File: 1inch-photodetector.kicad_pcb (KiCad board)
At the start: 4 copper layers, 25 x 25 mm, 21 parts, among them J1 Conn_01x03, J2 Conn_Coaxial, U1 ADA4898-2, U2 LT3032-12

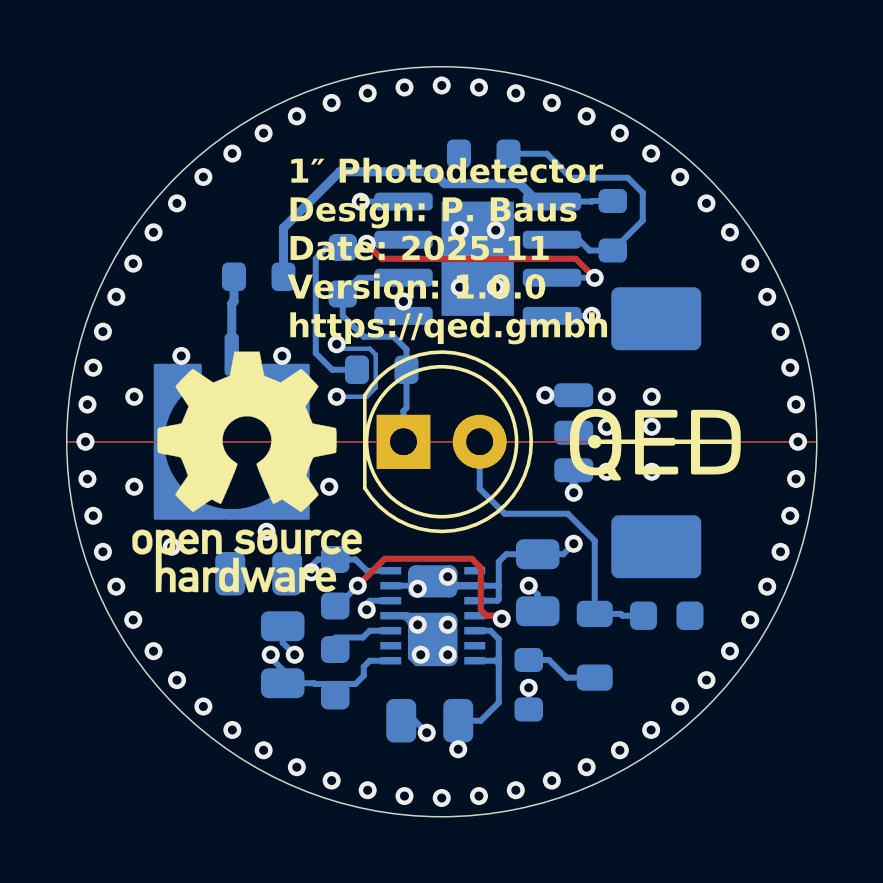
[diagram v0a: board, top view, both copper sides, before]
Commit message: Removed GND-Earth connection
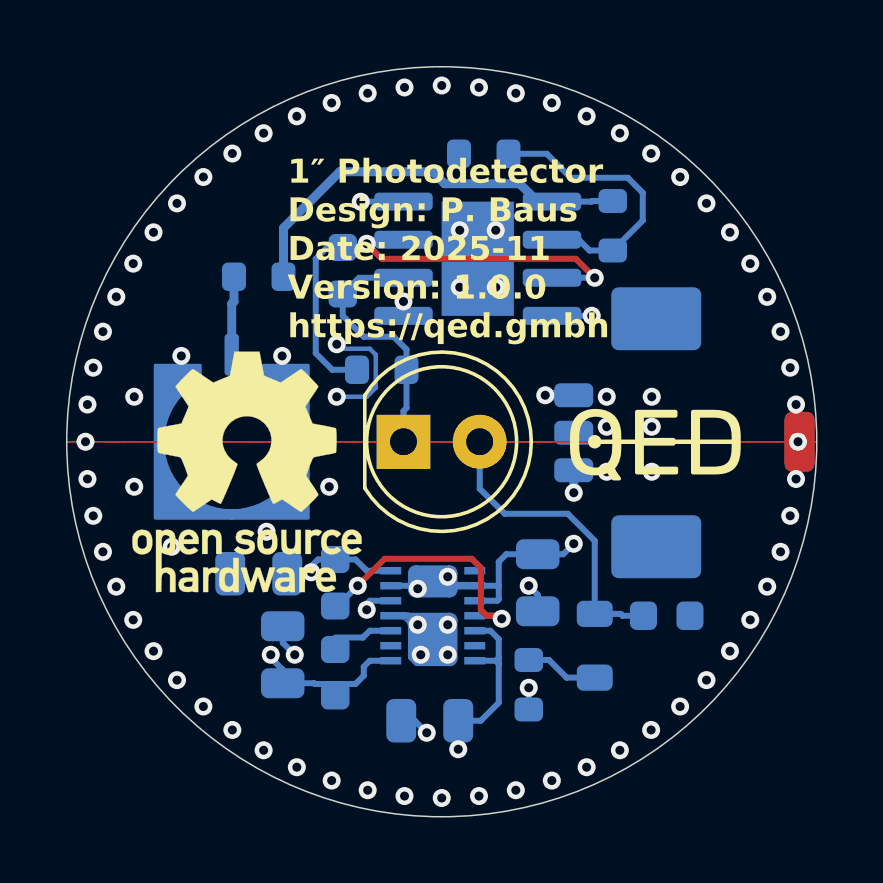
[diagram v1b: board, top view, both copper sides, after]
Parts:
- added H1: MountingHole_Pad, Connector_Wire:SolderWirePad_1x01_SMD_1x2mm, F.Cu at (161.9, 100.0)
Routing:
- net GND: vias 84 -> 24
- net Earth: vias 0 -> 60
- added copper zone on B.Cu, net Earth
- added copper zone on F.Cu, net Earth
- added copper zone on In1.Cu, net Earth
- added copper zone on In2.Cu, net Earth

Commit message: Increased size to 25.4 mm
- Added optional jumpers to connect GND to Earth
- Added more ground stitching vias
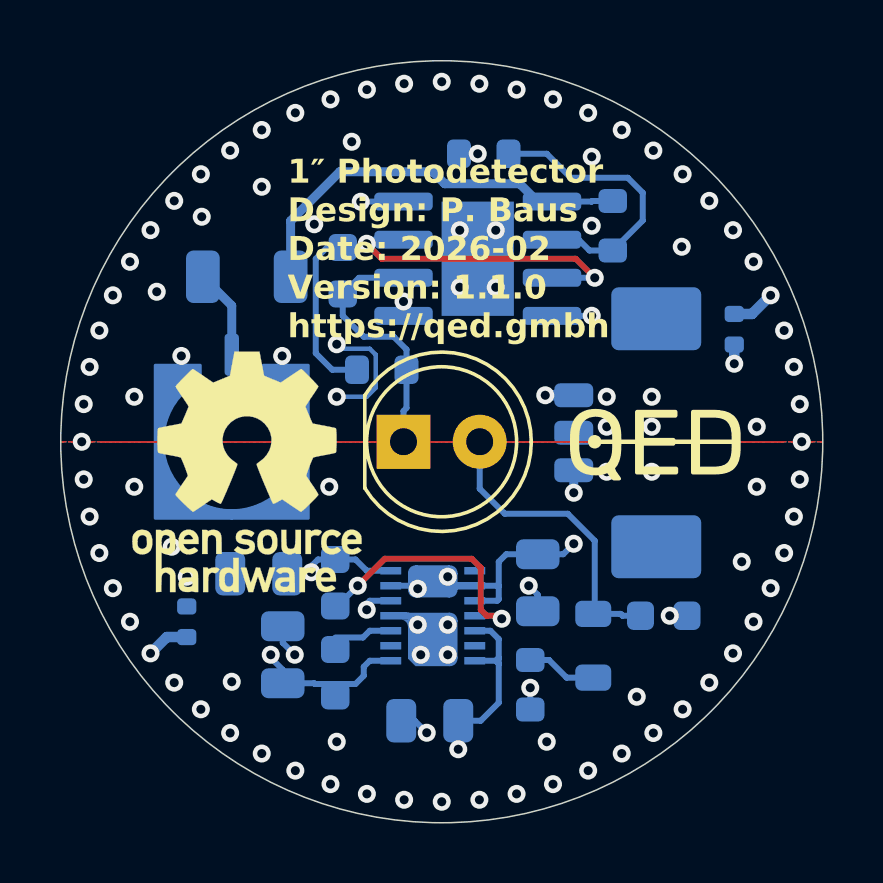
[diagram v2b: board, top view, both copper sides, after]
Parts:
- removed H1: MountingHole_Pad, Connector_Wire:SolderWirePad_1x01_SMD_1x2mm
- added JP1: Jumper_2_Open, Resistor_SMD:R_0402_1005Metric, B.Cu at (159.8, 96.2)
- added JP2: Jumper_2_Open, Resistor_SMD:R_0402_1005Metric, B.Cu at (141.5, 106.0)
- C3, C4: value C -> 100p
- C5, C6, C7, C8: value C -> 10u
- R1: footprint Resistor_SMD:R_0603_1608Metric -> Resistor_SMD:R_1206_3216Metric
- U2: value LT3032-12 -> LT3032IDE-12
- moved R1 0.40 mm to (143.5, 94.5)
- moved C2 0.10 mm to (157.4, 105.8)
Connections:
- net Net-(J1-Pin_1) renamed /V+
- net Net-(J1-Pin_3) renamed /V-
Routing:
- net Earth: track 0.00 -> 2.90 mm
- net GND: track 8.60 -> 10.4 mm, vias 24 -> 42
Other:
- board size 25 x 25 mm -> 25.4 x 25.4 mm
- board text added: "+"
- board text added: "-"
- board text added: "1″ Photodetector Design: P. Baus Date: 2026-02 Version: 1.1.0 https://qed.gmbh"
- board text added: "Clear aperture 22.9 mm (Thorlabs SM1RR retaining ring)"
- board text added: "G"
- board text removed: "1″ Photodetector Design: P. Baus Date: 2025-11 Version: 1.0.0 https://qed.gmbh"
